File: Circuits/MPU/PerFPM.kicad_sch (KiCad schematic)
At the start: 46 parts, among them Q4 SI4421DY, Q5 MMBTA92, Q6 MMBTA92, U10 ADA4805-2ARMZ, U7 LT1715, U8 ADA4805-2ARMZ, U9 ADA4805-2ARMZ

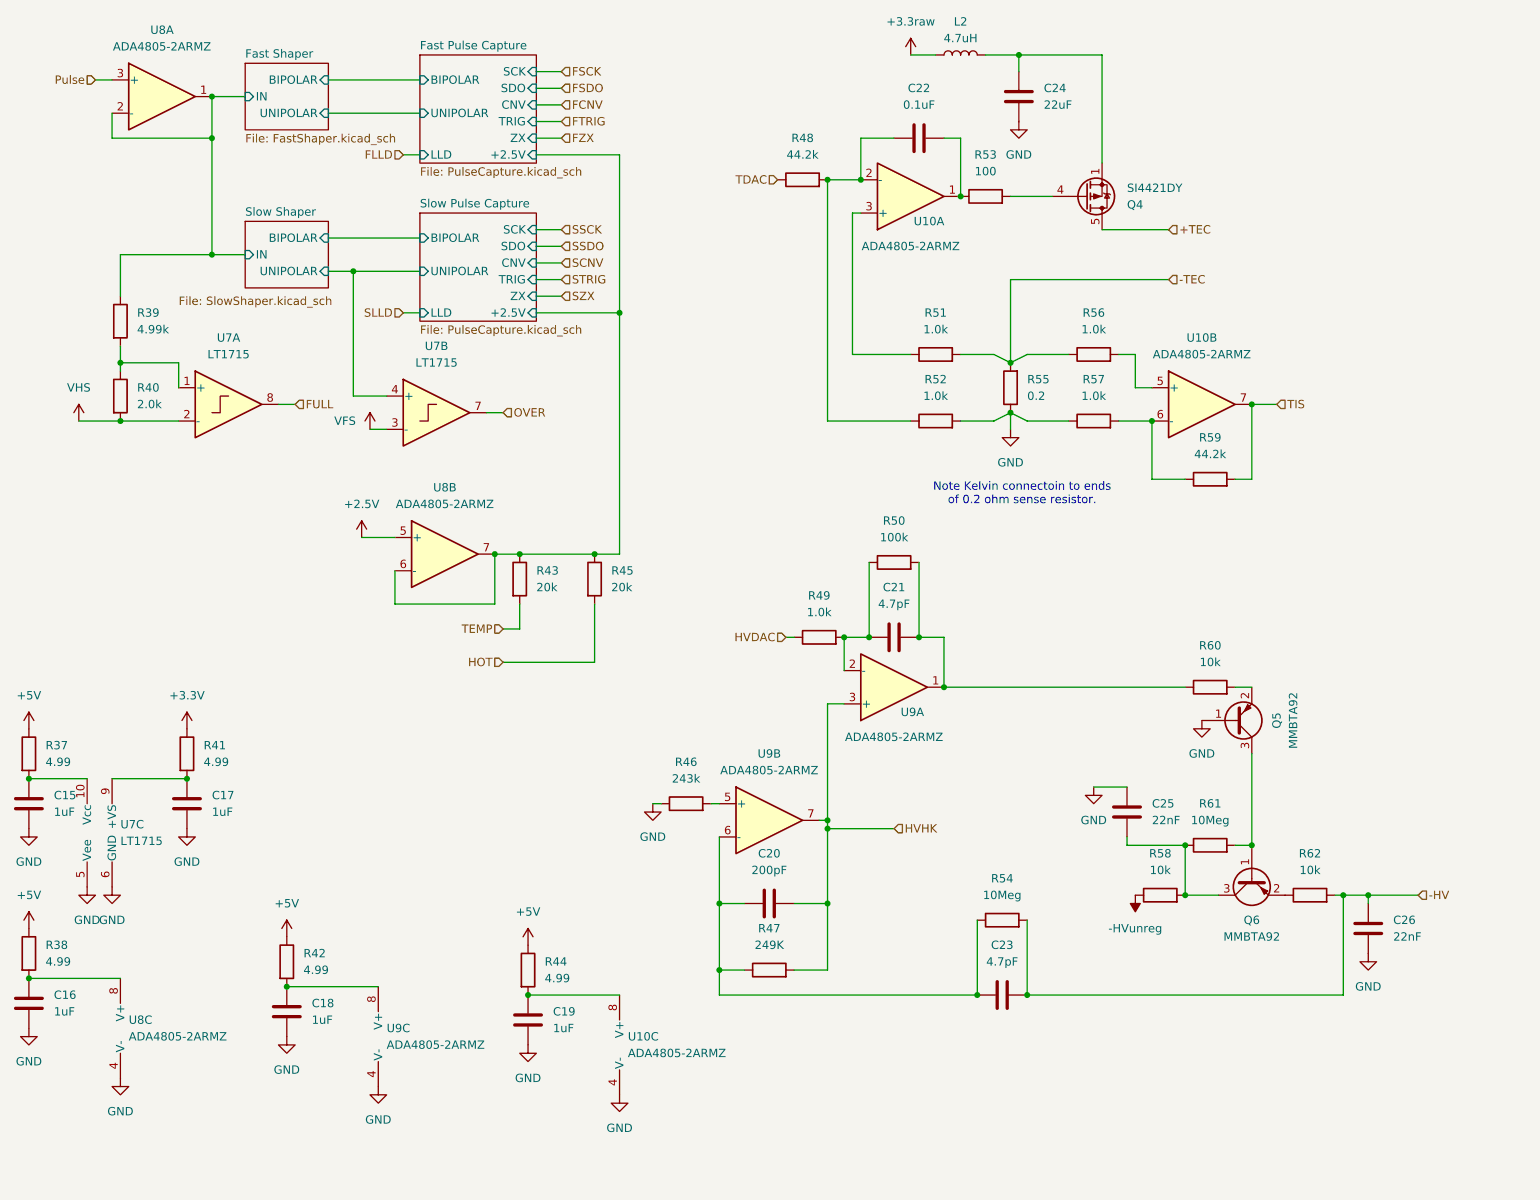
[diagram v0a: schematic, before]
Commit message: Pulse buffer power fix. HV reg compensation fix.
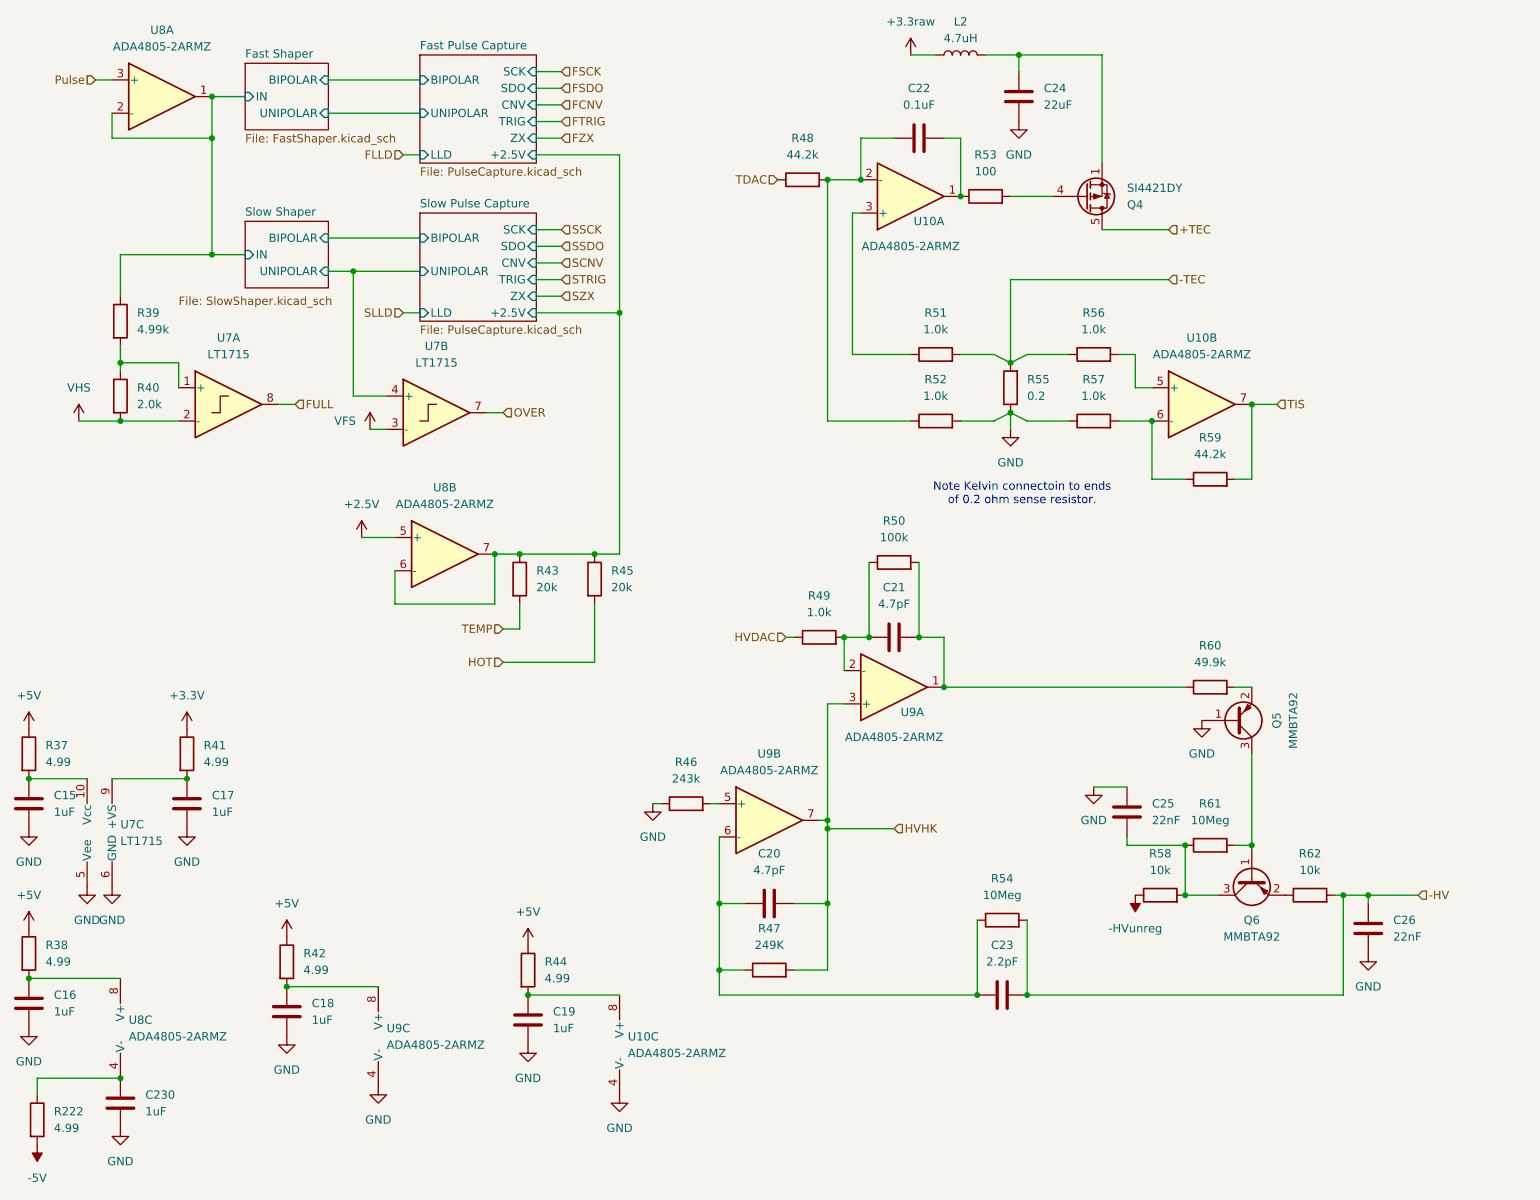
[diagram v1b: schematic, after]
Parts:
- added C230: 1uF, Capacitor_SMD:C_0805_2012Metric, symbol QuERI_symbols:C
- added R222: 4.99, Resistor_SMD:R_0603_1608Metric, symbol QuERI_symbols:Rlowp
- C20: value 200pF -> 4.7pF
- C23: value 4.7pF -> 2.2pF; footprint Capacitor_SMD:C_1210_3225Metric -> Capacitor_SMD:C_1206_3216Metric
- R60: value 10k -> 49.9k
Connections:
- net GND: now also C230.2; no longer U8.4 (V-)
- new net: C230.1, R222.1, U8.4 (V-)
- new net -5V: R222.2

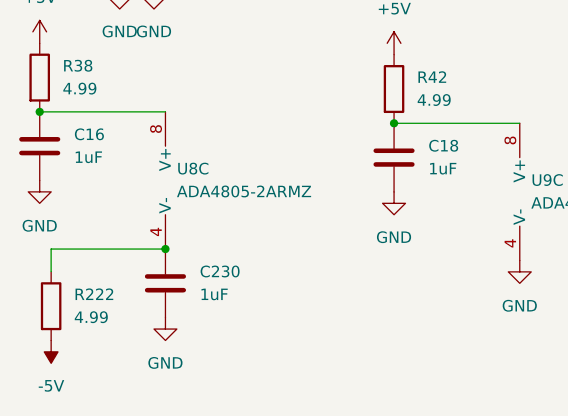
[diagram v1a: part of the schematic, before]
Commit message: fix MPU temp sensor bias
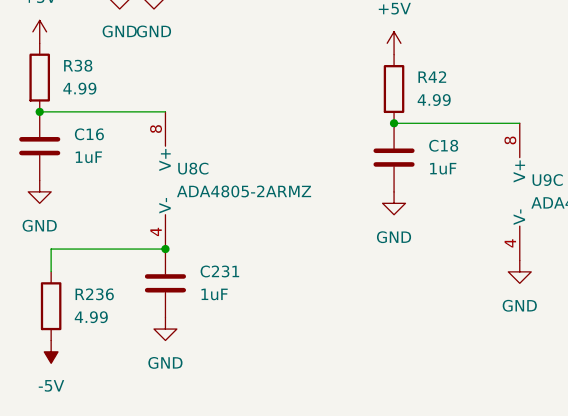
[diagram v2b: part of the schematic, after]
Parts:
- renumbered C230 to C231, R222 to R236
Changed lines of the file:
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@@
 		(title "QuERI MPU")
 		(date "2024-07-10")
-		(rev "RR4")
+		(rev "Draft")
 		(company "Noqsi Aerospace Ltd")
 		(comment 1 "15 Blanchard Avenue, Billerica MA 01821")
@@
 		(dnp no)
 		(fields_autoplaced yes)
-		(property "Reference" "R222"
+		(property "Reference" "R236"
 			(at 39.37 185.42 0)
 			(effects
@@
 		(dnp no)
 		(fields_autoplaced yes)
-		(property "Reference" "C230"
+		(property "Reference" "C231"
 			(at 53.34 182.88 0)
 			(effects
@@
 		(dnp no)
 		(fields_autoplaced yes)
-		(property "Reference" "#PWR042"
+		(property "Reference" "#PWR068"
 			(at 49.53 194.31 0)
 			(effects
@@
 		(on_board yes)
 		(dnp no)
-		(property "Reference" "#PWR0347"
+		(property "Reference" "#PWR0348"
 			(at 36.83 186.69 0)
 			(effects

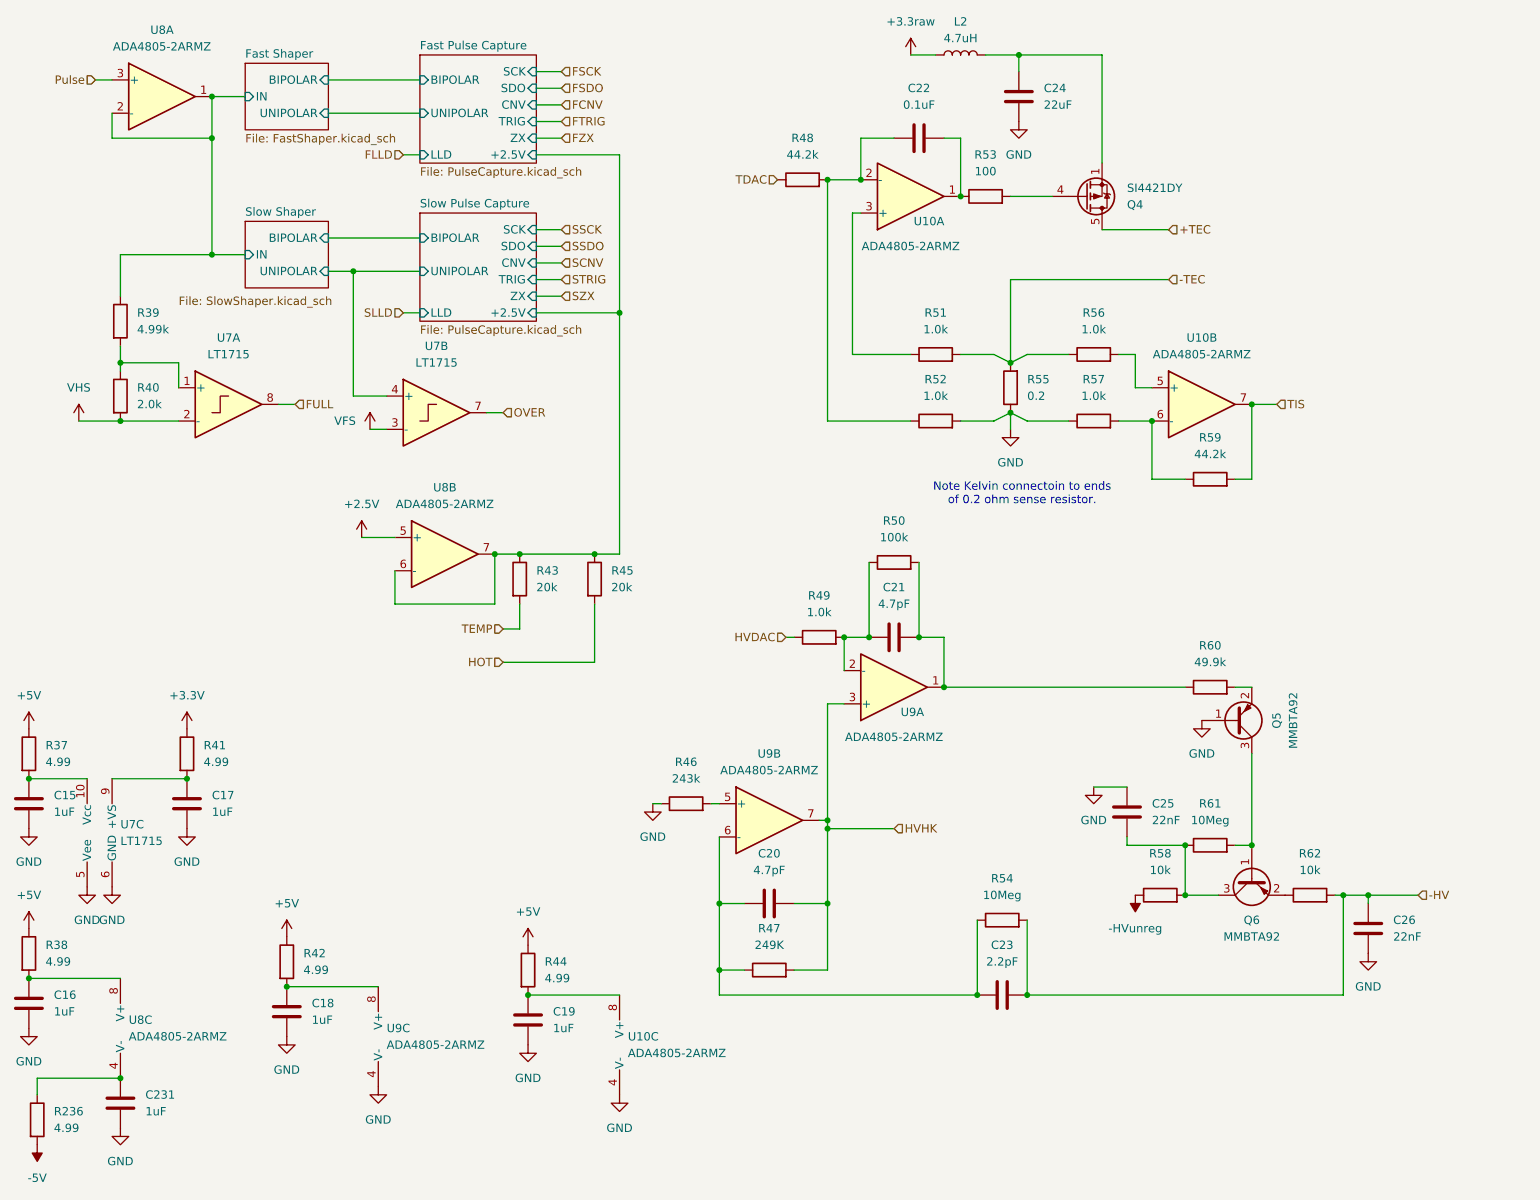
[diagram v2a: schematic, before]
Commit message: Files changed due to KiCAD update
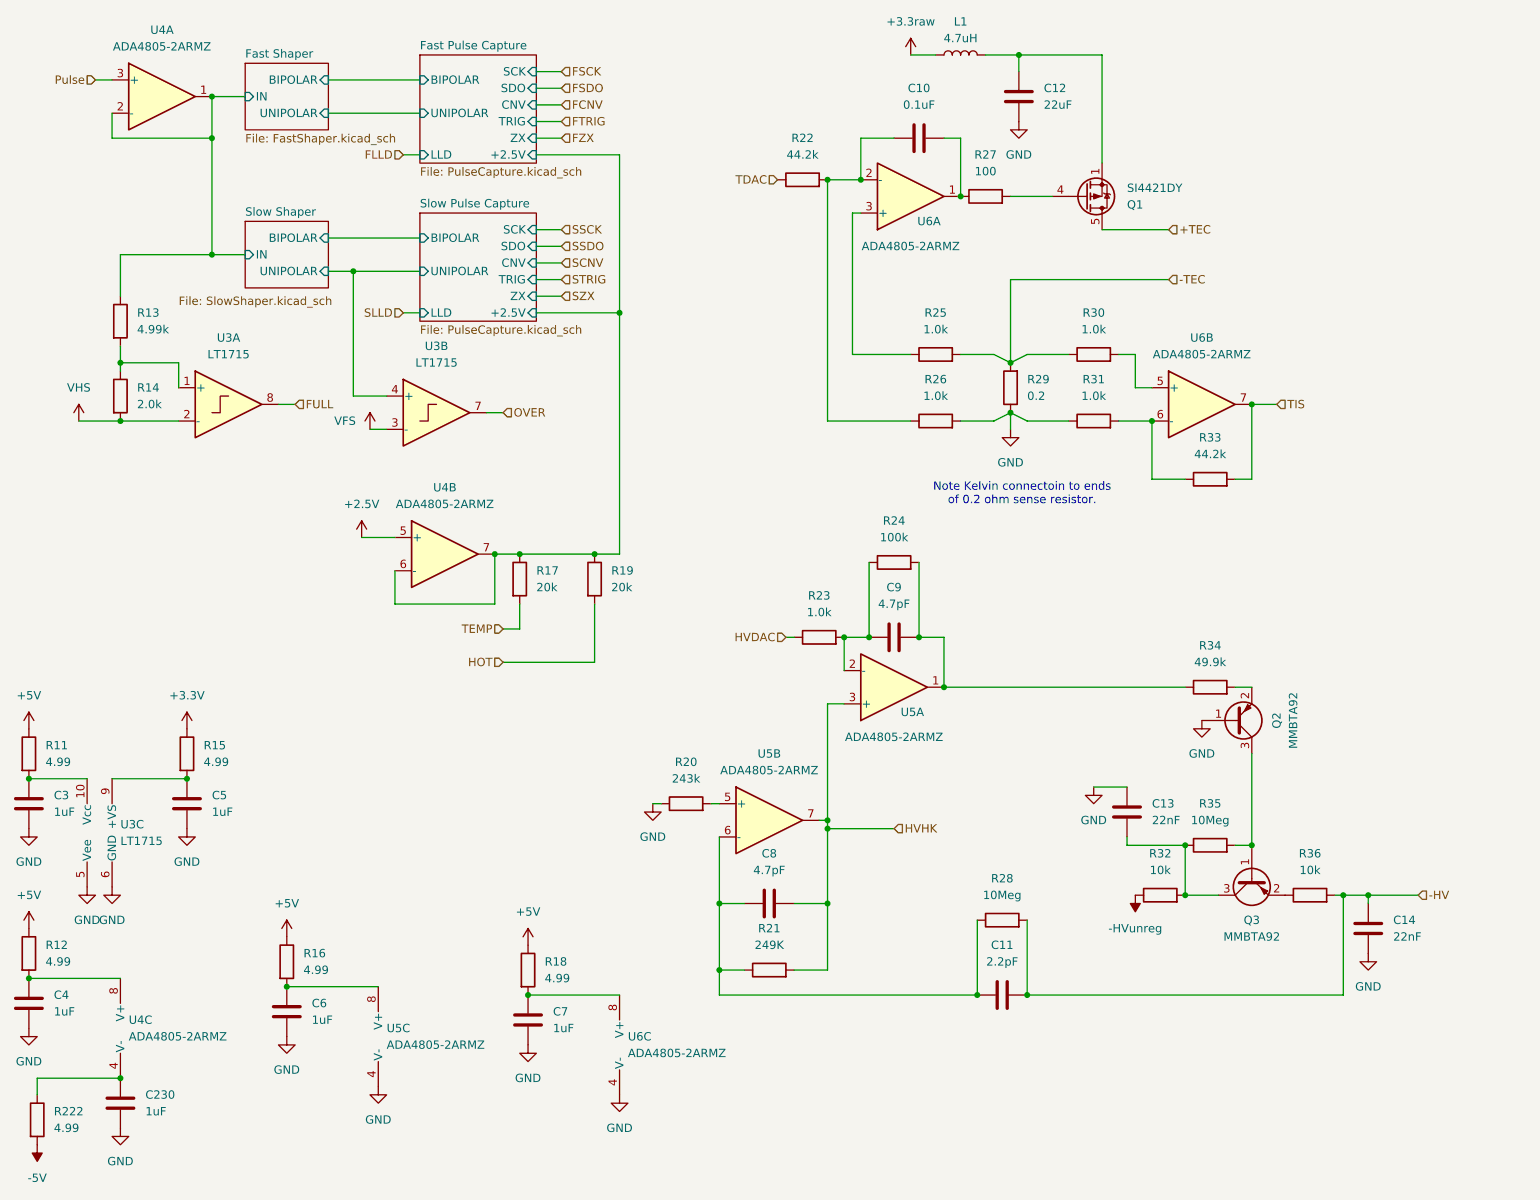
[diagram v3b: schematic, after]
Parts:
- renumbered C22 to C10, C23 to C11, C24 to C12, C25 to C13, C26 to C14, C231 to C230, C15 to C3, C16 to C4, C17 to C5, C18 to C6, C19 to C7, C20 to C8, C21 to C9, L2 to L1, Q4 to Q1, Q5 to Q2, Q6 to Q3, R37 to R11, R38 to R12, R39 to R13, R40 to R14, R41 to R15, R42 to R16, R43 to R17, R44 to R18, R45 to R19, R46 to R20, R47 to R21, R48 to R22, R236 to R222, R49 to R23, R50 to R24, R51 to R25, R52 to R26, R53 to R27, R54 to R28, R55 to R29, R56 to R30, R57 to R31, R58 to R32, R59 to R33, R60 to R34, R61 to R35, R62 to R36, U7 to U3, U8 to U4, U9 to U5, U10 to U6
